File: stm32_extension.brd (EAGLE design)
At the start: 1 part

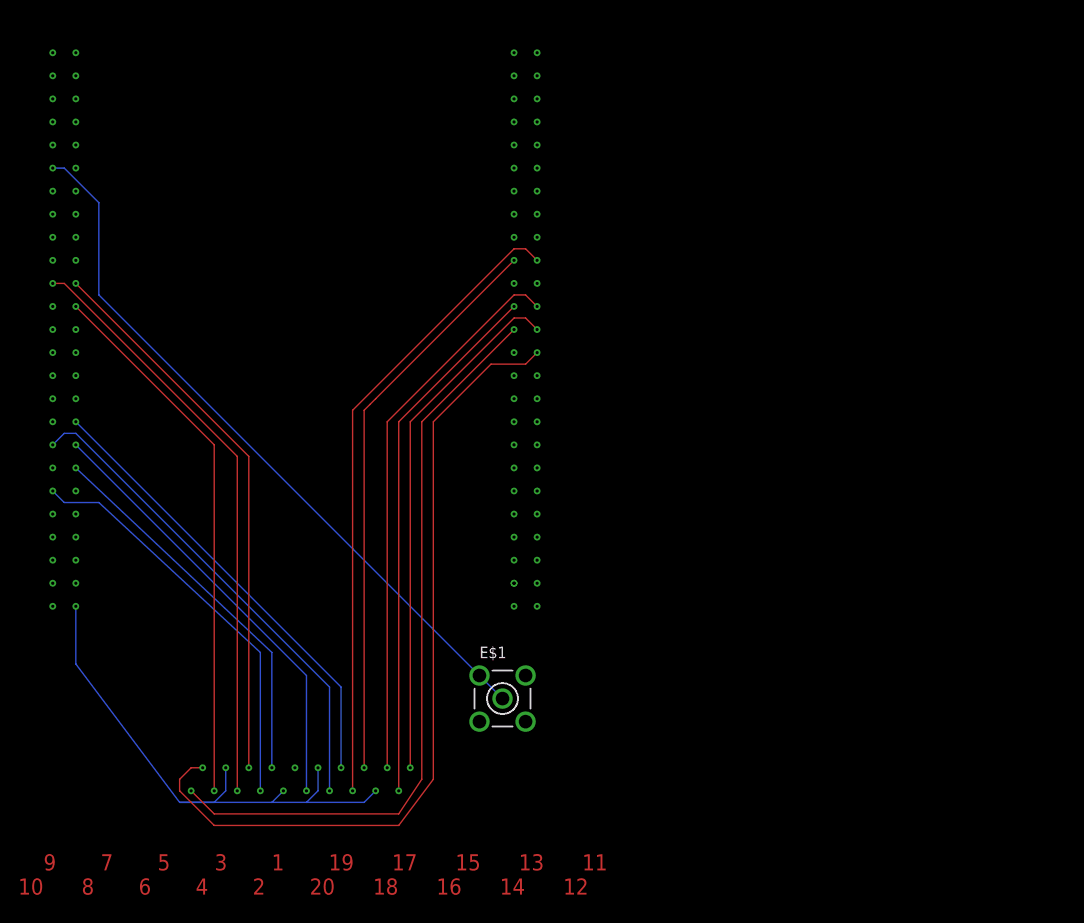
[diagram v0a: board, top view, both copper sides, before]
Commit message: Replaced char arrays with int arrays. Added MWE for testing. Board design + Pinout.
Replaced char arrays with more flexible int arrays.
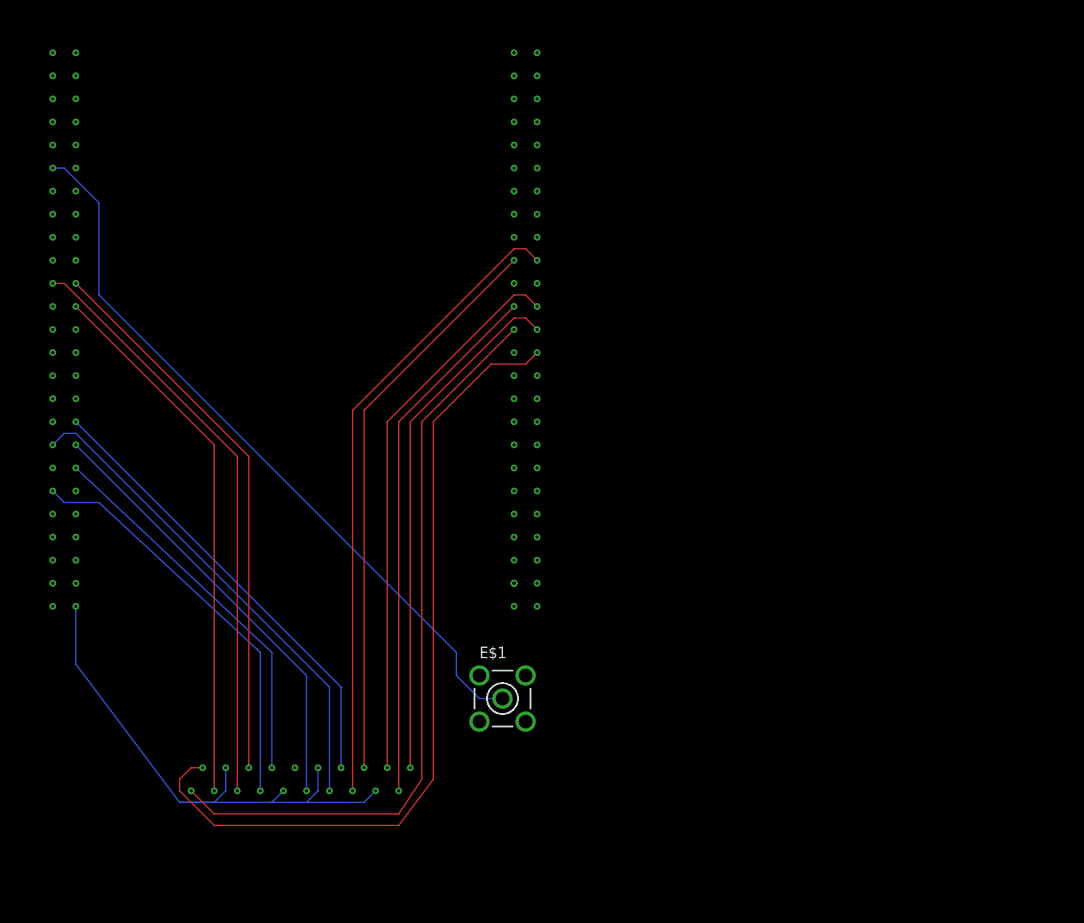
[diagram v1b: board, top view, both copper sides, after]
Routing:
- net S$59: track 79.7 -> 81.2 mm
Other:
- board text removed: "9 7 5 3 1 19 17 15 13 11 10 8 6 4 2 20 18 16 14 12"
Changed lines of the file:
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@@
 <layer number="43" name="vRestrict" color="2" fill="10" visible="yes" active="yes"/>
 <layer number="44" name="Drills" color="7" fill="1" visible="no" active="yes"/>
-<layer number="45" name="Holes" color="7" fill="1" visible="no" active="yes"/>
+<layer number="45" name="Holes" color="7" fill="1" visible="yes" active="yes"/>
 <layer number="46" name="Milling" color="3" fill="1" visible="no" active="yes"/>
 <layer number="47" name="Measures" color="7" fill="1" visible="no" active="yes"/>
@@
 <board>
 <plain>
-<text x="-29.21" y="-19.05" size="1.778" layer="1">    9       7       5       3       1       19      17      15      13      11
-10      8       6       4       2       20      18      16      14      12  </text>
 <dimension x1="-33.02" y1="73.66" x2="-33.02" y2="-11.43" x3="-31.75" y3="31.115" textsize="1.778" layer="1"/>
-<dimension x1="33.02" y1="80.01" x2="-29.21" y2="80.01" x3="1.905" y3="80.01" textsize="1.778" layer="1"/>
-<dimension x1="-25.4" y1="74.93" x2="27.94" y2="74.93" x3="1.27" y3="74.93" textsize="1.778" layer="1"/>
-<dimension x1="36.83" y1="73.66" x2="36.83" y2="12.7" x3="36.83" y3="43.18" textsize="1.778" layer="1"/>
+<dimension x1="-25.4" y1="80.01" x2="27.94" y2="80.01" x3="1.27" y3="80.01" textsize="1.778" layer="1"/>
+<dimension x1="-25.4" y1="76.2" x2="-22.86" y2="76.2" x3="-24.13" y3="76.2" textsize="1.778" layer="1"/>
+<dimension x1="27.94" y1="10.16" x2="34.29" y2="10.16" x3="31.115" y3="8.89" textsize="1.778" layer="1"/>
+<dimension x1="35.56" y1="73.66" x2="35.56" y2="12.7" x3="36.83" y3="43.18" textsize="1.778" layer="1"/>
+<dimension x1="-25.4" y1="-7.62" x2="-25.4" y2="-13.97" x3="-24.13" y3="-10.795" textsize="1.778" layer="1"/>
 </plain>
 <attributes>
@@
 <wire x1="-24.13" y1="60.96" x2="-20.32" y2="57.15" width="0.1524" layer="16"/>
 <wire x1="-20.32" y1="57.15" x2="-20.32" y2="46.99" width="0.1524" layer="16"/>
-<wire x1="-20.32" y1="46.99" x2="24.13" y2="2.54" width="0.1524" layer="16"/>
+<wire x1="-20.32" y1="46.99" x2="19.05" y2="7.62" width="0.1524" layer="16"/>
+<wire x1="19.05" y1="7.62" x2="19.05" y2="5.08" width="0.1524" layer="16"/>
+<wire x1="19.05" y1="5.08" x2="21.59" y2="2.54" width="0.1524" layer="16"/>
+<wire x1="21.59" y1="2.54" x2="24.13" y2="2.54" width="0.1524" layer="16"/>
 </signal>
 <signal name="S$60">
@@
 </drawing>
 <compatibility>
-<note version="6.3" minversion="6.2.2" severity="warning">
-Since Version 6.2.2 text objects can contain more than one line,
-which will not be processed correctly with this version.
-</note>
 <note version="8.2" severity="warning">
 Since Version 8.2, Eagle supports online libraries. The ids

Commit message: Ground plane and 50 ohm BNC added.
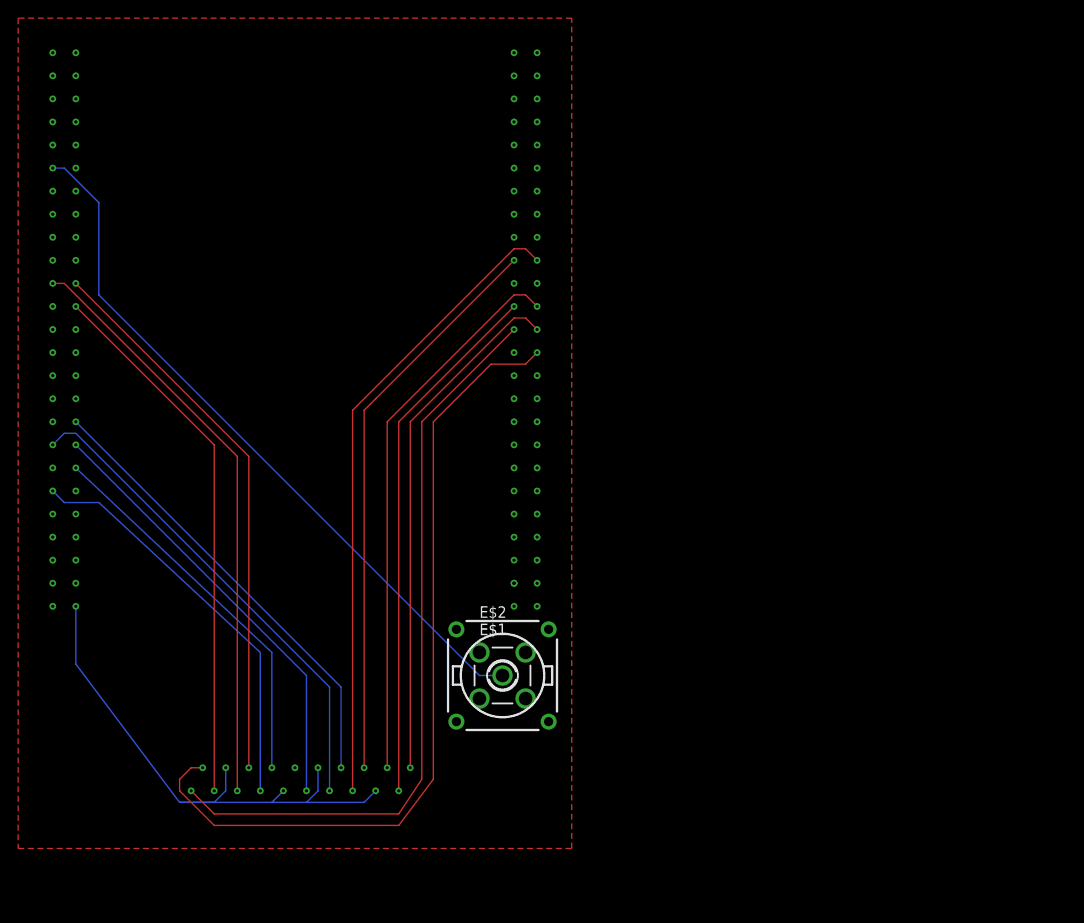
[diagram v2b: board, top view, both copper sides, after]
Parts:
- added E$2: (no value), con-coax:A1944
- moved E$1 2.54 mm to (24.1, 5.08)
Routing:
- net S$59: track 81.2 -> 78.6 mm
- added copper zone on layer 1, net GND
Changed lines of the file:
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@@
 <board>
 <plain>
-<dimension x1="-33.02" y1="73.66" x2="-33.02" y2="-11.43" x3="-31.75" y3="31.115" textsize="1.778" layer="1"/>
-<dimension x1="-25.4" y1="80.01" x2="27.94" y2="80.01" x3="1.27" y3="80.01" textsize="1.778" layer="1"/>
-<dimension x1="-25.4" y1="76.2" x2="-22.86" y2="76.2" x3="-24.13" y3="76.2" textsize="1.778" layer="1"/>
-<dimension x1="27.94" y1="10.16" x2="34.29" y2="10.16" x3="31.115" y3="8.89" textsize="1.778" layer="1"/>
-<dimension x1="35.56" y1="73.66" x2="35.56" y2="12.7" x3="36.83" y3="43.18" textsize="1.778" layer="1"/>
-<dimension x1="-25.4" y1="-7.62" x2="-25.4" y2="-13.97" x3="-24.13" y3="-10.795" textsize="1.778" layer="1"/>
 </plain>
 <attributes>
@@
 </autorouter>
 <elements>
-<element name="E$1" library="con-coax" library_urn="urn:adsk.eagle:library:133" package="LTI-SASF54GT" value="" x="24.13" y="2.54"/>
+<element name="E$1" library="con-coax" library_urn="urn:adsk.eagle:library:133" package="LTI-SASF54GT" value="" x="24.13" y="5.08"/>
+<element name="E$2" library="con-coax" library_urn="urn:adsk.eagle:library:133" package="A1944" value="" x="24.13" y="5.08"/>
 </elements>
 <signals>
@@
 <wire x1="-24.13" y1="60.96" x2="-20.32" y2="57.15" width="0.1524" layer="16"/>
 <wire x1="-20.32" y1="57.15" x2="-20.32" y2="46.99" width="0.1524" layer="16"/>
-<wire x1="-20.32" y1="46.99" x2="19.05" y2="7.62" width="0.1524" layer="16"/>
-<wire x1="19.05" y1="7.62" x2="19.05" y2="5.08" width="0.1524" layer="16"/>
-<wire x1="19.05" y1="5.08" x2="21.59" y2="2.54" width="0.1524" layer="16"/>
-<wire x1="21.59" y1="2.54" x2="24.13" y2="2.54" width="0.1524" layer="16"/>
+<wire x1="-20.32" y1="46.99" x2="21.59" y2="5.08" width="0.1524" layer="16"/>
+<wire x1="21.59" y1="5.08" x2="24.13" y2="5.08" width="0.1524" layer="16"/>
 </signal>
 <signal name="S$60">
@@
 <via x="25.4" y="12.7" extent="1-16" drill="0.35"/>
 </signal>
+<signal name="GND">
+<polygon width="0.2" layer="1" isolate="0.3048">
+<vertex x="31.75" y="-13.97"/>
+<vertex x="31.75" y="77.47"/>
+<vertex x="-29.21" y="77.47"/>
+<vertex x="-29.21" y="-13.97"/>
+</polygon>
+</signal>
 </signals>
